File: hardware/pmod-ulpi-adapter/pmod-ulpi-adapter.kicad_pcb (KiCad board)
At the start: 2 copper layers, 16.5 x 39.1 mm, 10 parts, among them J1 PMOD-2x6-MALE, J2 PMOD-2x6-MALE, J3 ULPI, J4 Conn_01x02

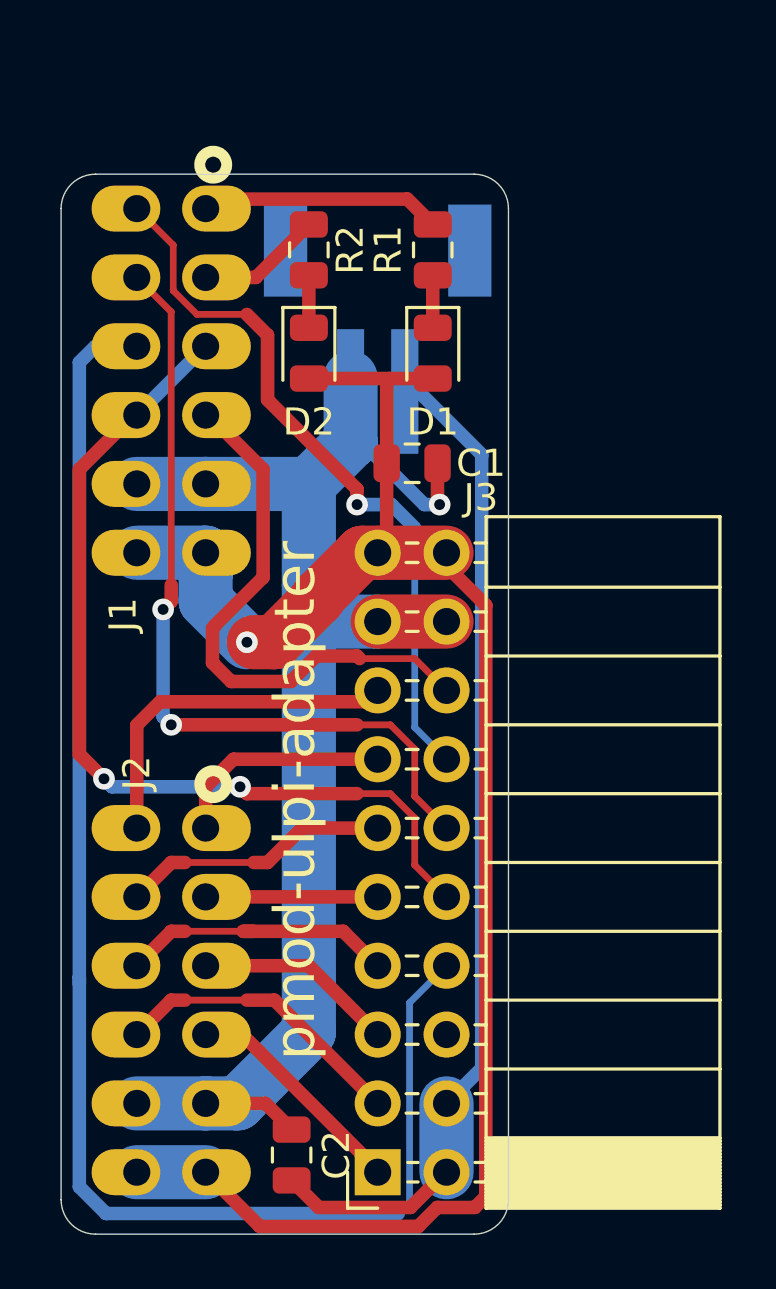
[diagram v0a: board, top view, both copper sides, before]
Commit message: pmod-ulpi-adapter: Mar2021A release, swapped pmod connectors for more clock option
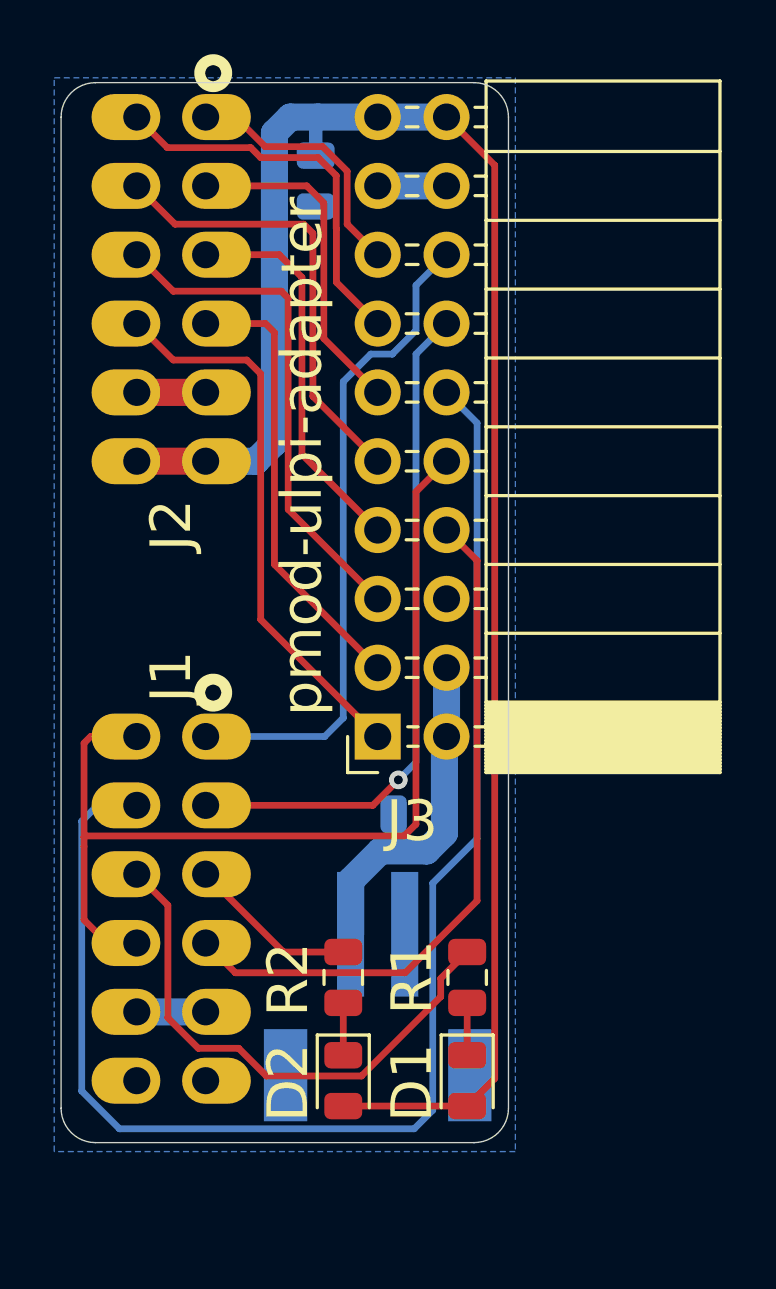
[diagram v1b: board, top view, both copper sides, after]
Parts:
- C1, C2: moved to B.Cu
- moved J4 27.4 mm to (171.4, 115.6), turned to 0 degrees
- moved D1 26.9 mm to (174.8, 117.3)
- moved D2 26.9 mm to (170.2, 117.3)
- moved R1 26.9 mm to (174.8, 113.5)
- moved R2 26.9 mm to (170.2, 113.5)
- moved J2 26.2 mm to (163.8, 88.1)
- moved J1 19.5 mm to (163.8, 110.9)
- moved J3 16.1 mm to (171.4, 104.6)
- moved C2 13.4 mm to (173.0, 107.4), turned to 0 degrees
- moved C1 11.0 mm to (169.2, 84.1), turned to 90 degrees
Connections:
- J1 pad 1: /BLUE -> /STP
- J1 pad 12: +3V3 -> Net-(J1-Pad12)
- J1 pad 2: /YELLOW -> /NXT
- J1 pad 3: /CLKOUT -> /YELLOW
- J1 pad 4: /STP -> /RESET
- J1 pad 6: +3V3 -> Net-(J1-Pad6)
- J1 pad 7: /NXT -> /CLKOUT
- J1 pad 9: /RESET -> /BLUE
- J2 pad 1: /DATA6 -> /DATA7
- J2 pad 10: /DATA1 -> /DATA0
- J2 pad 2: /DATA4 -> /DATA5
- J2 pad 3: /DATA2 -> /DATA3
- J2 pad 4: /DATA0 -> /DATA1
- J2 pad 7: /DATA7 -> /DATA6
- J2 pad 8: /DATA5 -> /DATA4
- J2 pad 9: /DATA3 -> /DATA2
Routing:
- net GND: track 53.1 -> 7.62 mm, vias 1 -> 0
- net /RESET: track 55.1 -> 25.7 mm
- net +5V: track 37.7 -> 12.3 mm
- net /DIR: track 30.0 -> 53.7 mm, vias 2 -> 0
- net /DATA0: track 8.50 -> 20.5 mm
- net /DATA2: track 7.40 -> 18.7 mm
- net /BLUE: track 8.92 -> 20.0 mm
- net /DATA4: track 6.35 -> 16.6 mm
- net /DATA6: track 8.29 -> 14.3 mm
- net /DATA1: track 11.0 -> 16.6 mm
- net /DATA3: track 10.3 -> 14.4 mm
- net /STP: track 20.7 -> 24.5 mm
- net /DATA7: track 13.2 -> 9.60 mm
- net /CLKOUT: track 33.8 -> 37.2 mm, vias 2 -> 0
- net /NXT: track 26.9 -> 25.1 mm
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- added copper zone on B.Cu, net GND
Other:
- board text added: "@TomKeddie Mar 2021 A"
- board text removed: "@TomKeddie Mar2021"
